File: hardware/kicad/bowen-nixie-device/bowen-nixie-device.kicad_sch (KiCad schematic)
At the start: 119 parts, among them J1 Conn_01x02_Pin, J2 Conn_01x02_Pin, J3 Conn_01x04_Pin, Q1 SS8050, Q10 MMBTA42, Q11 MMBTA42, Q12 MMBTA42, Q13 MMBTA42, Q14 MMBTA42, Q15 MMBTA42, Q16 MMBTA42, Q17 MMBTA42, Q18 MMBTA42, Q19 MMBTA42, Q2 MPSA92, Q20 MMBTA42, Q21 MMBTA42, Q22 MMBTA42, Q23 MMBTA42, Q24 MMBTA42, Q25 MMBTA42, Q26 MMBTA42, Q27 MMBTA42, Q28 MMBTA42, Q29 MMBTA42, Q3 SS8050, Q30 MMBTA42, Q31 MMBTA42, Q32 MMBTA42, Q33 MMBTA42, Q34 MMBTA42, Q35 MMBTA42, Q36 MMBTA42, Q37 MMBTA42, Q38 MMBTA42, Q39 MMBTA42, Q4 MPSA92, Q40 MMBTA42, Q41 MMBTA42, Q42 MMBTA42, Q43 MMBTA42, Q44 MMBTA42, Q45 MMBTA42, Q46 MMBTA42, Q47 MMBTA42, Q48 MMBTA42, Q5 SS8050, Q6 MPSA92, Q7 SS8050, Q8 MPSA92, Q9 MMBTA42, U1 MOUDLE-SEEEDUINO-XIAO-ESP32C3, U11 NCH8200HV, U2 74HC595, U3 74HC595, U4 74HC595, U5 74HC595, U6 74HC595

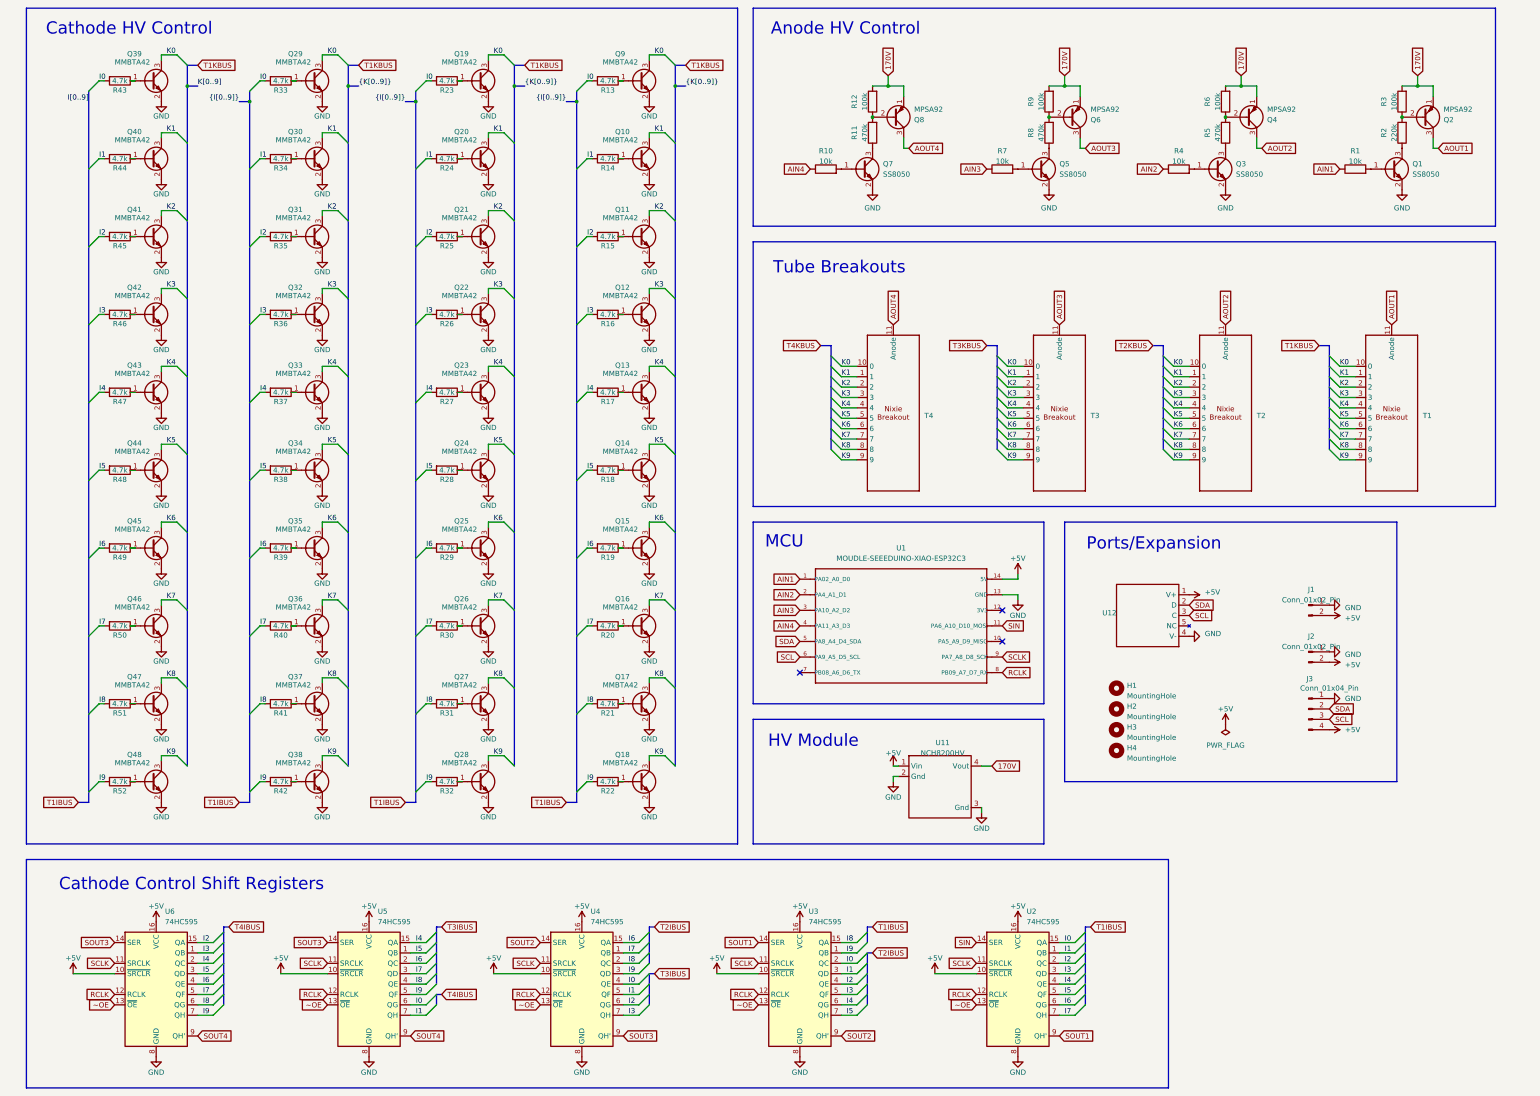
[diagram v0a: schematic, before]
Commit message: schematic passing ERC
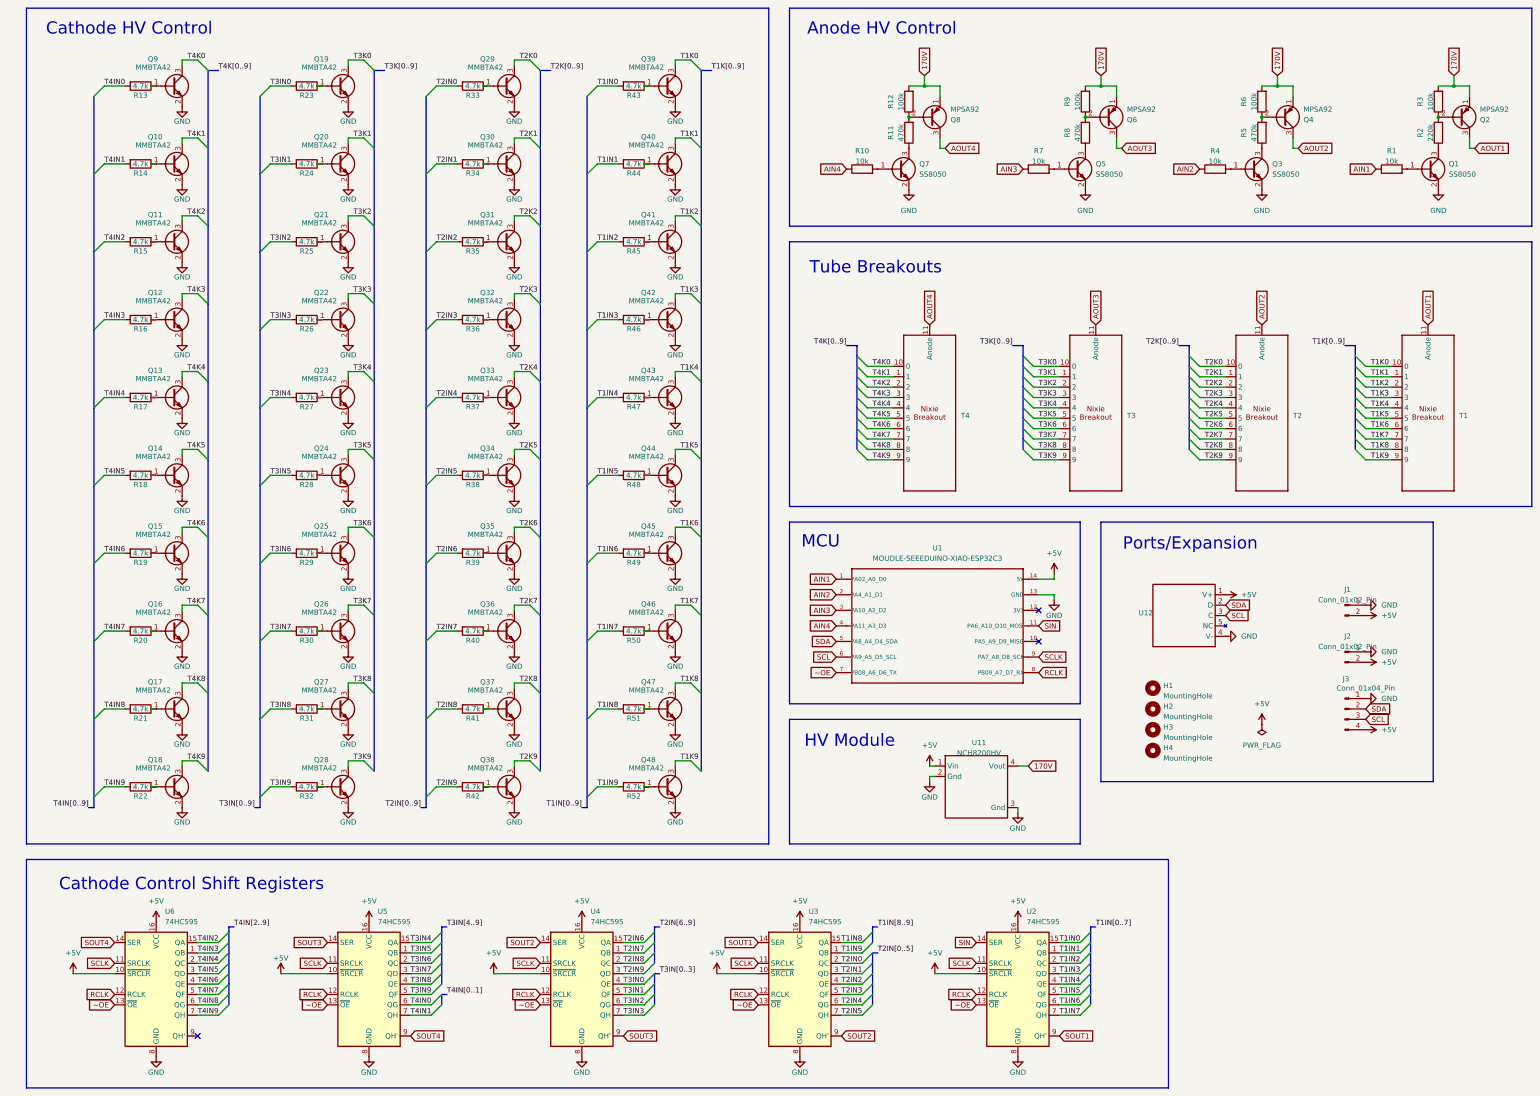
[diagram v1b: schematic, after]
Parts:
- R13, R14, R15, R16, R17, R18, R19, R20, R21, R22, R23, R24, R25, R26, R27, R28, R29, R30, R31, R32, R33, R34, R35, R36, R37, R38, R39, R40, R41, R42, R43, R44, R45, R46, R47, R48, R49, R50, R51, R52: footprint NONIK0:R_0603_1608Metric -> Resistor_SMD:R_0603_1608Metric
- U1: footprint MOUDLE14P-SMD-2.54-21X17.8MM -> Nixie:MOUDLE14P-SMD-2.54-21X17.8MM
- U2, U3, U4, U5, U6: footprint (none) -> Package_SO:SOIC-16_4.55x10.3mm_P1.27mm
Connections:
- net SOUT3: no longer U6.14 (SER)
- net SOUT4: now also U6.14 (SER); no longer U6.9 (QH')
- net ~OE: now also U1.7 (PB08_A6_D6_TX)
- removed net I0: R13.2, R23.2, R33.2, R43.2, U2.15 (QA), U3.2 (QC), U4.4 (QE), U5.6 (QG)
- removed net I1: R14.2, R24.2, R34.2, R44.2, U2.1 (QB), U3.3 (QD), U4.5 (QF), U5.7 (QH)
- removed net I2: R15.2, R25.2, R35.2, R45.2, U2.2 (QC), U3.4 (QE), U4.6 (QG), U6.15 (QA)
- removed net I3: R16.2, R26.2, R36.2, R46.2, U2.3 (QD), U3.5 (QF), U4.7 (QH), U6.1 (QB)
- removed net I4: R17.2, R27.2, R37.2, R47.2, U2.4 (QE), U3.6 (QG), U5.15 (QA), U6.2 (QC)
- removed net I5: R18.2, R28.2, R38.2, R48.2, U2.5 (QF), U3.7 (QH), U5.1 (QB), U6.3 (QD)
- removed net I6: R19.2, R29.2, R39.2, R49.2, U2.6 (QG), U4.15 (QA), U5.2 (QC), U6.4 (QE)
- removed net I7: R20.2, R30.2, R40.2, R50.2, U2.7 (QH), U4.1 (QB), U5.3 (QD), U6.5 (QF)
- removed net I8: R21.2, R31.2, R41.2, R51.2, U3.15 (QA), U4.2 (QC), U5.4 (QE), U6.6 (QG)
- removed net I9: R22.2, R32.2, R42.2, R52.2, U3.1 (QB), U4.3 (QD), U5.5 (QF), U6.7 (QH)
- removed net K0: Q19.3 (C), Q29.3 (C), Q39.3 (C), Q9.3 (C), T1.10 (0), T2.10 (0), T3.10 (0), T4.10 (0)
- removed net K1: Q10.3 (C), Q20.3 (C), Q30.3 (C), Q40.3 (C), T1.1, T2.1, T3.1, T4.1
- removed net K2: Q11.3 (C), Q21.3 (C), Q31.3 (C), Q41.3 (C), T1.2, T2.2, T3.2, T4.2
- removed net K3: Q12.3 (C), Q22.3 (C), Q32.3 (C), Q42.3 (C), T1.3, T2.3, T3.3, T4.3
- removed net K4: Q13.3 (C), Q23.3 (C), Q33.3 (C), Q43.3 (C), T1.4, T2.4, T3.4, T4.4
- removed net K5: Q14.3 (C), Q24.3 (C), Q34.3 (C), Q44.3 (C), T1.5, T2.5, T3.5, T4.5
- removed net K6: Q15.3 (C), Q25.3 (C), Q35.3 (C), Q45.3 (C), T1.6, T2.6, T3.6, T4.6
- removed net K7: Q16.3 (C), Q26.3 (C), Q36.3 (C), Q46.3 (C), T1.7, T2.7, T3.7, T4.7
- removed net K8: Q17.3 (C), Q27.3 (C), Q37.3 (C), Q47.3 (C), T1.8, T2.8, T3.8, T4.8
- removed net K9: Q18.3 (C), Q28.3 (C), Q38.3 (C), Q48.3 (C), T1.9, T2.9, T3.9, T4.9
- new net T1IN0: R43.2, U2.15 (QA)
- new net T1IN1: R44.2, U2.1 (QB)
- new net T1IN2: R45.2, U2.2 (QC)
- new net T1IN3: R46.2, U2.3 (QD)
- new net T1IN4: R47.2, U2.4 (QE)
- new net T1IN5: R48.2, U2.5 (QF)
- new net T1IN6: R49.2, U2.6 (QG)
- new net T1IN7: R50.2, U2.7 (QH)
- new net T1IN8: R51.2, U3.15 (QA)
- new net T1IN9: R52.2, U3.1 (QB)
- new net T1K0: Q39.3 (C), T1.10 (0)
- new net T1K1: Q40.3 (C), T1.1
- new net T1K2: Q41.3 (C), T1.2
- new net T1K3: Q42.3 (C), T1.3
- new net T1K4: Q43.3 (C), T1.4
- new net T1K5: Q44.3 (C), T1.5
- new net T1K6: Q45.3 (C), T1.6
- new net T1K7: Q46.3 (C), T1.7
- new net T1K8: Q47.3 (C), T1.8
- new net T1K9: Q48.3 (C), T1.9
- new net T2IN0: R33.2, U3.2 (QC)
- new net T2IN1: R34.2, U3.3 (QD)
- new net T2IN2: R35.2, U3.4 (QE)
- new net T2IN3: R36.2, U3.5 (QF)
- new net T2IN4: R37.2, U3.6 (QG)
- new net T2IN5: R38.2, U3.7 (QH)
- new net T2IN6: R39.2, U4.15 (QA)
- new net T2IN7: R40.2, U4.1 (QB)
- new net T2IN8: R41.2, U4.2 (QC)
- new net T2IN9: R42.2, U4.3 (QD)
- new net T2K0: Q29.3 (C), T2.10 (0)
- new net T2K1: Q30.3 (C), T2.1
- new net T2K2: Q31.3 (C), T2.2
- new net T2K3: Q32.3 (C), T2.3
- new net T2K4: Q33.3 (C), T2.4
- new net T2K5: Q34.3 (C), T2.5
- new net T2K6: Q35.3 (C), T2.6
- new net T2K7: Q36.3 (C), T2.7
- new net T2K8: Q37.3 (C), T2.8
- new net T2K9: Q38.3 (C), T2.9
- new net T3IN0: R23.2, U4.4 (QE)
- new net T3IN1: R24.2, U4.5 (QF)
- new net T3IN2: R25.2, U4.6 (QG)
- new net T3IN3: R26.2, U4.7 (QH)
- new net T3IN4: R27.2, U5.15 (QA)
- new net T3IN5: R28.2, U5.1 (QB)
- new net T3IN6: R29.2, U5.2 (QC)
- new net T3IN7: R30.2, U5.3 (QD)
- new net T3IN8: R31.2, U5.4 (QE)
- new net T3IN9: R32.2, U5.5 (QF)
- new net T3K0: Q19.3 (C), T3.10 (0)
- new net T3K1: Q20.3 (C), T3.1
- new net T3K2: Q21.3 (C), T3.2
- new net T3K3: Q22.3 (C), T3.3
- new net T3K4: Q23.3 (C), T3.4
- new net T3K5: Q24.3 (C), T3.5
- new net T3K6: Q25.3 (C), T3.6
- new net T3K7: Q26.3 (C), T3.7
- new net T3K8: Q27.3 (C), T3.8
- new net T3K9: Q28.3 (C), T3.9
- new net T4IN0: R13.2, U5.6 (QG)
- new net T4IN1: R14.2, U5.7 (QH)
- new net T4IN2: R15.2, U6.15 (QA)
- new net T4IN3: R16.2, U6.1 (QB)
- new net T4IN4: R17.2, U6.2 (QC)
- new net T4IN5: R18.2, U6.3 (QD)
- new net T4IN6: R19.2, U6.4 (QE)
- new net T4IN7: R20.2, U6.5 (QF)
- new net T4IN8: R21.2, U6.6 (QG)
- new net T4IN9: R22.2, U6.7 (QH)
- new net T4K0: Q9.3 (C), T4.10 (0)
- new net T4K1: Q10.3 (C), T4.1
- new net T4K2: Q11.3 (C), T4.2
- new net T4K3: Q12.3 (C), T4.3
- new net T4K4: Q13.3 (C), T4.4
- new net T4K5: Q14.3 (C), T4.5
- new net T4K6: Q15.3 (C), T4.6
- new net T4K7: Q16.3 (C), T4.7
- new net T4K8: Q17.3 (C), T4.8
- new net T4K9: Q18.3 (C), T4.9
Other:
- moved on the sheet: H1, H2, H3, H4, J1, J2, J3, Q1, Q10, Q11, Q12, Q13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

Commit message: rough initial layout
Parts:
- R1, R10, R11, R12, R2, R3, R4, R5, R6, R7, R8, R9: footprint Resistor_THT:R_Axial_DIN0207_L6.3mm_D2.5mm_P7.62mm_Horizontal -> Resistor_SMD:R_0603_1608Metric
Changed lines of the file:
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@@
 			)
 		)
-		(property "Footprint" "Resistor_THT:R_Axial_DIN0207_L6.3mm_D2.5mm_P7.62mm_Horizontal"
+		(property "Footprint" "Resistor_SMD:R_0603_1608Metric"
 			(at 350.52 57.658 90)
 			(effects
@@
 			)
 		)
-		(property "Footprint" "Resistor_THT:R_Axial_DIN0207_L6.3mm_D2.5mm_P7.62mm_Horizontal"
+		(property "Footprint" "Resistor_SMD:R_0603_1608Metric"
 			(at 234.188 46.99 90)
 			(effects
@@
 			)
 		)
-		(property "Footprint" "Resistor_THT:R_Axial_DIN0207_L6.3mm_D2.5mm_P7.62mm_Horizontal"
+		(property "Footprint" "Resistor_SMD:R_0603_1608Metric"
 			(at 320.548 46.99 90)
 			(effects
@@
 			)
 		)
-		(property "Footprint" "Resistor_THT:R_Axial_DIN0207_L6.3mm_D2.5mm_P7.62mm_Horizontal"
+		(property "Footprint" "Resistor_SMD:R_0603_1608Metric"
 			(at 363.728 46.99 90)
 			(effects
@@
 			)
 		)
-		(property "Footprint" "Resistor_THT:R_Axial_DIN0207_L6.3mm_D2.5mm_P7.62mm_Horizontal"
+		(property "Footprint" "Resistor_SMD:R_0603_1608Metric"
 			(at 363.728 39.37 90)
 			(effects
@@
 			)
 		)
-		(property "Footprint" "Resistor_THT:R_Axial_DIN0207_L6.3mm_D2.5mm_P7.62mm_Horizontal"
+		(property "Footprint" "Resistor_SMD:R_0603_1608Metric"
 			(at 277.368 39.37 90)
 			(effects
@@
 			)
 		)
-		(property "Footprint" "Resistor_THT:R_Axial_DIN0207_L6.3mm_D2.5mm_P7.62mm_Horizontal"
+		(property "Footprint" "Resistor_SMD:R_0603_1608Metric"
 			(at 220.98 57.658 90)
 			(effects
@@
 			)
 		)
-		(property "Footprint" "Resistor_THT:R_Axial_DIN0207_L6.3mm_D2.5mm_P7.62mm_Horizontal"
+		(property "Footprint" "Resistor_SMD:R_0603_1608Metric"
 			(at 320.548 39.37 90)
 			(effects
@@
 			)
 		)
-		(property "Footprint" "Resistor_THT:R_Axial_DIN0207_L6.3mm_D2.5mm_P7.62mm_Horizontal"
+		(property "Footprint" "Resistor_SMD:R_0603_1608Metric"
 			(at 307.34 57.658 90)
 			(effects
@@
 			)
 		)
-		(property "Footprint" "Resistor_THT:R_Axial_DIN0207_L6.3mm_D2.5mm_P7.62mm_Horizontal"
+		(property "Footprint" "Resistor_SMD:R_0603_1608Metric"
 			(at 234.188 39.37 90)
 			(effects
@@
 			)
 		)
-		(property "Footprint" "Resistor_THT:R_Axial_DIN0207_L6.3mm_D2.5mm_P7.62mm_Horizontal"
+		(property "Footprint" "Resistor_SMD:R_0603_1608Metric"
 			(at 277.368 46.99 90)
 			(effects
@@
 			)
 		)
-		(property "Footprint" "Resistor_THT:R_Axial_DIN0207_L6.3mm_D2.5mm_P7.62mm_Horizontal"
+		(property "Footprint" "Resistor_SMD:R_0603_1608Metric"
 			(at 264.16 57.658 90)
 			(effects

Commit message: bowen progress
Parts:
- Q1, Q3, Q5, Q7: value SS8050 -> MMBTA42; symbol Transistor_BJT:SS8050 -> Transistor_BJT:MMBTA42
- Q2, Q4, Q6, Q8: value MPSA92 -> MMBTA92; footprint Package_TO_SOT_THT:TO-92_Inline -> PCM_Package_TO_SOT_SMD_AKL:SOT-23; symbol Transistor_BJT:MPSA92 -> PCM_Transistor_BJT_AKL:MMBTA92
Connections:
- net 170V: now also Q2.2 (E), Q4.2 (E), Q6.2 (E), Q8.2 (E); no longer Q2.1 (E), Q4.1 (E), Q6.1 (E), Q8.1 (E)
- net at R11.2, R12.1: now also Q8.1 (B); no longer Q8.2 (B)
- net at R5.2, R6.1: now also Q4.1 (B); no longer Q4.2 (B)
- net at R2.2, R3.1: now also Q2.1 (B); no longer Q2.2 (B)
- net at R8.2, R9.1: now also Q6.1 (B); no longer Q6.2 (B)

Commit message: trace progress, gnd plane and most traces
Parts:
- T1, T2, T3, T4, U12: value ~ -> (none)
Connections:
- net AIN1: now also U1.4 (PA11_A3_D3); no longer U1.1 (PA02_A0_D0)
- net AIN2: now also U1.3 (PA10_A2_D2); no longer U1.2 (PA4_A1_D1)
- net AIN3: now also U1.2 (PA4_A1_D1); no longer U1.3 (PA10_A2_D2)
- net AIN4: now also U1.1 (PA02_A0_D0); no longer U1.4 (PA11_A3_D3)

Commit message: layout final
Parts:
- U1: footprint Nixie:MOUDLE14P-SMD-2.54-21X17.8MM -> Nixie:XIAO-ESP32-C3-DIP
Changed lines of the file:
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@@
 			)
 		)
-		(property "Footprint" "Nixie:MOUDLE14P-SMD-2.54-21X17.8MM"
+		(property "Footprint" "Nixie:XIAO-ESP32-C3-DIP"
 			(at 240.03 167.64 0)
 			(hide yes)

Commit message: bowen updates
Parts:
- added H5: MountingHole, MountingHole:MountingHole_2.2mm_M2_DIN965_Pad, symbol Mechanical:MountingHole
- added J4: Qwiic/Stemma QT, Connector_JST:JST_SH_BM04B-SRSS-TB_1x04-1MP_P1.00mm_Vertical, symbol HPDL-1414:JST_04_Fixed
- added J5: Conn_01x03_Pin, Connector_PinSocket_2.54mm:PinSocket_1x03_P2.54mm_Vertical, symbol Connector:Conn_01x03_Pin
- H1, H2, H3, H4: footprint MountingHole:MountingHole_2.2mm_M2 -> MountingHole:MountingHole_2.2mm_M2_DIN965_Pad
- R2: value 220k -> 470k
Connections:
- net +5V: now also J4.3, J5.3 (Pin_3)
- net GND: now also J4.4, J5.1 (Pin_1)
- net SCL: now also J4.1
- net SDA: now also J4.2
- net EXT: now reaches U1.10 (PA5_A9_D9_MISO)
- net EXT: now also J5.2 (Pin_2)
- no-connect marks 3 -> 2
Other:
- moved on the sheet: J1, J2, J3
